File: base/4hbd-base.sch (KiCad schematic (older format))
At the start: 13 parts

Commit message: draft 0.02 of mosfets_sens_isol.sch
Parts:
- gave numbers to parts that had none: 13
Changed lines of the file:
@@
 $EndSheet
 $Comp
-L GNDD #PWR?
+L GNDD #PWR8
 U 1 1 5A1C4DF7
 P 8900 6000
-F 0 "#PWR?" H 8900 5750 50  0001 C CNN
+F 0 "#PWR8" H 8900 5750 50  0001 C CNN
 F 1 "GNDD" H 8900 5875 50  0000 C CNN
 F 2 "" H 8900 6000 50  0001 C CNN
@@
 $EndComp
 $Comp
-L GNDD #PWR?
+L GNDD #PWR7
 U 1 1 5A1C5052
 P 8900 3500
-F 0 "#PWR?" H 8900 3250 50  0001 C CNN
+F 0 "#PWR7" H 8900 3250 50  0001 C CNN
 F 1 "GNDD" H 8900 3375 50  0000 C CNN
 F 2 "" H 8900 3500 50  0001 C CNN
@@
 $EndComp
 $Comp
-L GNDD #PWR?
+L GNDD #PWR5
 U 1 1 5A1C5445
 P 4800 6300
-F 0 "#PWR?" H 4800 6050 50  0001 C CNN
+F 0 "#PWR5" H 4800 6050 50  0001 C CNN
 F 1 "GNDD" H 4800 6175 50  0000 C CNN
 F 2 "" H 4800 6300 50  0001 C CNN
@@
 $EndComp
 $Comp
-L GNDD #PWR?
+L GNDD #PWR4
 U 1 1 5A1C7749
 P 4800 3800
-F 0 "#PWR?" H 4800 3550 50  0001 C CNN
+F 0 "#PWR4" H 4800 3550 50  0001 C CNN
 F 1 "GNDD" H 4800 3675 50  0000 C CNN
 F 2 "" H 4800 3800 50  0001 C CNN
@@
 $EndComp
 $Comp
-L GNDD #PWR?
+L GNDD #PWR6
 U 1 1 5A1D2700
 P 8400 4800
-F 0 "#PWR?" H 8400 4550 50  0001 C CNN
+F 0 "#PWR6" H 8400 4550 50  0001 C CNN
 F 1 "GNDD" H 8400 4675 50  0000 C CNN
 F 2 "" H 8400 4800 50  0001 C CNN
@@
 $EndComp
 $Comp
-L Screw_Terminal_01x02 J?
+L Screw_Terminal_01x02 J11
 U 1 1 5A1D730D
 P 10800 5400
-F 0 "J?" H 10800 5500 50  0000 C CNN
+F 0 "J11" H 10800 5500 50  0000 C CNN
 F 1 "Screw_Terminal_01x02" H 10800 5200 50  0000 C CNN
 F 2 "" H 10800 5400 50  0001 C CNN
@@
 $EndComp
 $Comp
-L GNDD #PWR?
+L GNDD #PWR10
 U 1 1 5A1D7E7F
 P 10500 5500
-F 0 "#PWR?" H 10500 5250 50  0001 C CNN
+F 0 "#PWR10" H 10500 5250 50  0001 C CNN
 F 1 "GNDD" H 10500 5375 50  0000 C CNN
 F 2 "" H 10500 5500 50  0001 C CNN
@@
 $EndSheet
 $Comp
-L Conn_01x08 J?
+L Conn_01x08 J13
 U 1 1 5A1E2A64
 P 10900 2700
-F 0 "J?" H 10900 3100 50  0000 C CNN
+F 0 "J13" H 10900 3100 50  0000 C CNN
 F 1 "Conn_01x08" H 10900 2200 50  0000 C CNN
 F 2 "" H 10900 2700 50  0001 C CNN
@@
 $EndComp
 $Comp
-L GNDD #PWR?
+L GNDD #PWR11
 U 1 1 5A1E3D1F
 P 10600 2500
-F 0 "#PWR?" H 10600 2250 50  0001 C CNN
+F 0 "#PWR11" H 10600 2250 50  0001 C CNN
 F 1 "GNDD" H 10600 2375 50  0000 C CNN
 F 2 "" H 10600 2500 50  0001 C CNN
@@
 $EndComp
 $Comp
-L GNDD #PWR?
+L GNDD #PWR9
 U 1 1 5A1E950D
 P 10200 1600
-F 0 "#PWR?" H 10200 1350 50  0001 C CNN
+F 0 "#PWR9" H 10200 1350 50  0001 C CNN
 F 1 "GNDD" H 10200 1475 50  0000 C CNN
 F 2 "" H 10200 1600 50  0001 C CNN
@@
 Connection ~ 10400 5400
 $Comp
-L Conn_01x03 J?
+L Conn_01x03 J12
 U 1 1 5A1EF510
 P 10900 1100
-F 0 "J?" H 10900 1300 50  0000 C CNN
+F 0 "J12" H 10900 1300 50  0000 C CNN
 F 1 "Conn_01x03" H 10900 900 50  0000 C CNN
 F 2 "" H 10900 1100 50  0001 C CNN
@@
 	1400 7000 1200 7000
 $Comp
-L GNDPWR #PWR?
+L GNDPWR #PWR3
 U 1 1 5A1F43A1
 P 2800 6300
-F 0 "#PWR?" H 2800 6100 50  0001 C CNN
+F 0 "#PWR3" H 2800 6100 50  0001 C CNN
 F 1 "GNDPWR" H 2800 6170 50  0000 C CNN
 F 2 "" H 2800 6250 50  0001 C CNN
@@
 $EndComp
 $Comp
-L GNDPWR #PWR?
+L GNDPWR #PWR1
 U 1 1 5A1F4674
 P 1200 7100
-F 0 "#PWR?" H 1200 6900 50  0001 C CNN
+F 0 "#PWR1" H 1200 6900 50  0001 C CNN
 F 1 "GNDPWR" H 1200 6970 50  0000 C CNN
 F 2 "" H 1200 7050 50  0001 C CNN
@@
 $EndComp
 $Comp
-L GNDPWR #PWR?
+L GNDPWR #PWR2
 U 1 1 5A1F4ECF
 P 2800 3600
-F 0 "#PWR?" H 2800 3400 50  0001 C CNN
+F 0 "#PWR2" H 2800 3400 50  0001 C CNN
 F 1 "GNDPWR" H 2800 3470 50  0000 C CNN
 F 2 "" H 2800 3550 50  0001 C CNN
@@
 	2500 3300 3000 3300
 $Comp
-L Screw_Terminal_01x03 J?
+L Screw_Terminal_01x03 J9
 U 1 1 5A1F5775
 P 700 6700
-F 0 "J?" H 700 6900 50  0000 C CNN
+F 0 "J9" H 700 6900 50  0000 C CNN
 F 1 "Screw_Terminal_01x03" H 700 6500 50  0000 C CNN
 F 2 "" H 700 6700 50  0001 C CNN
@@
 	1100 3200 3000 3200
 $Comp
-L Screw_Terminal_01x04 J?
+L Screw_Terminal_01x04 J10
 U 1 1 5A1F75AA
 P 2400 1900
-F 0 "J?" H 2400 2100 50  0000 C CNN
+F 0 "J10" H 2400 2100 50  0000 C CNN
 F 1 "Screw_Terminal_01x04" H 2400 1600 50  0000 C CNN
 F 2 "" H 2400 1900 50  0001 C CNN
@@
 	2600 2000 3000 2000
 $Comp
-L Screw_Terminal_01x03 J?
+L Screw_Terminal_01x03 J1
 U 1 1 5A1F8DA5
 P 700 3400
-F 0 "J?" H 700 3600 50  0000 C CNN
+F 0 "J1" H 700 3600 50  0000 C CNN
 F 1 "Screw_Terminal_01x03" H 700 3200 50  0000 C CNN
 F 2 "" H 700 3400 50  0001 C CNN
@@
 $EndComp
 $Comp
-L Screw_Terminal_01x03 J?
+L Screw_Terminal_01x03 J2
 U 1 1 5A1F90C1
 P 700 3800
-F 0 "J?" H 700 4000 50  0000 C CNN
+F 0 "J2" H 700 4000 50  0000 C CNN
 F 1 "Screw_Terminal_01x03" H 700 3600 50  0000 C CNN
 F 2 "" H 700 3800 50  0001 C CNN
@@
 $EndComp
 $Comp
-L Screw_Terminal_01x03 J?
+L Screw_Terminal_01x03 J3
 U 1 1 5A1F93B8
 P 700 4200
-F 0 "J?" H 700 4400 50  0000 C CNN
+F 0 "J3" H 700 4400 50  0000 C CNN
 F 1 "Screw_Terminal_01x03" H 700 4000 50  0000 C CNN
 F 2 "" H 700 4200 50  0001 C CNN
@@
 $EndComp
 $Comp
-L Screw_Terminal_01x03 J?
+L Screw_Terminal_01x03 J4
 U 1 1 5A1F96AE
 P 700 4600
-F 0 "J?" H 700 4800 50  0000 C CNN
+F 0 "J4" H 700 4800 50  0000 C CNN
 F 1 "Screw_Terminal_01x03" H 700 4400 50  0000 C CNN
 F 2 "" H 700 4600 50  0001 C CNN
@@
 $EndComp
 $Comp
-L Screw_Terminal_01x03 J?
+L Screw_Terminal_01x03 J8
 U 1 1 5A1F99A1
 P 700 6000
-F 0 "J?" H 700 6200 50  0000 C CNN
+F 0 "J8" H 700 6200 50  0000 C CNN
 F 1 "Screw_Terminal_01x03" H 700 5800 50  0000 C CNN
 F 2 "" H 700 6000 50  0001 C CNN
@@
 $EndComp
 $Comp
-L Screw_Terminal_01x03 J?
+L Screw_Terminal_01x03 J7
 U 1 1 5A1F9CC3
 P 700 5600
-F 0 "J?" H 700 5800 50  0000 C CNN
+F 0 "J7" H 700 5800 50  0000 C CNN
 F 1 "Screw_Terminal_01x03" H 700 5400 50  0000 C CNN
 F 2 "" H 700 5600 50  0001 C CNN
@@
 $EndComp
 $Comp
-L Screw_Terminal_01x02 J?
+L Screw_Terminal_01x02 J5
 U 1 1 5A1FA292
 P 700 5000
-F 0 "J?" H 700 5100 50  0000 C CNN
+F 0 "J5" H 700 5100 50  0000 C CNN
 F 1 "Screw_Terminal_01x02" H 700 4800 50  0000 C CNN
 F 2 "" H 700 5000 50  0001 C CNN
@@
 $EndComp
 $Comp
-L Screw_Terminal_01x02 J?
+L Screw_Terminal_01x02 J6
 U 1 1 5A1FAA40
 P 700 5300
-F 0 "J?" H 700 5400 50  0000 C CNN
+F 0 "J6" H 700 5400 50  0000 C CNN
 F 1 "Screw_Terminal_01x02" H 700 5100 50  0000 C CNN
 F 2 "" H 700 5300 50  0001 C CNN

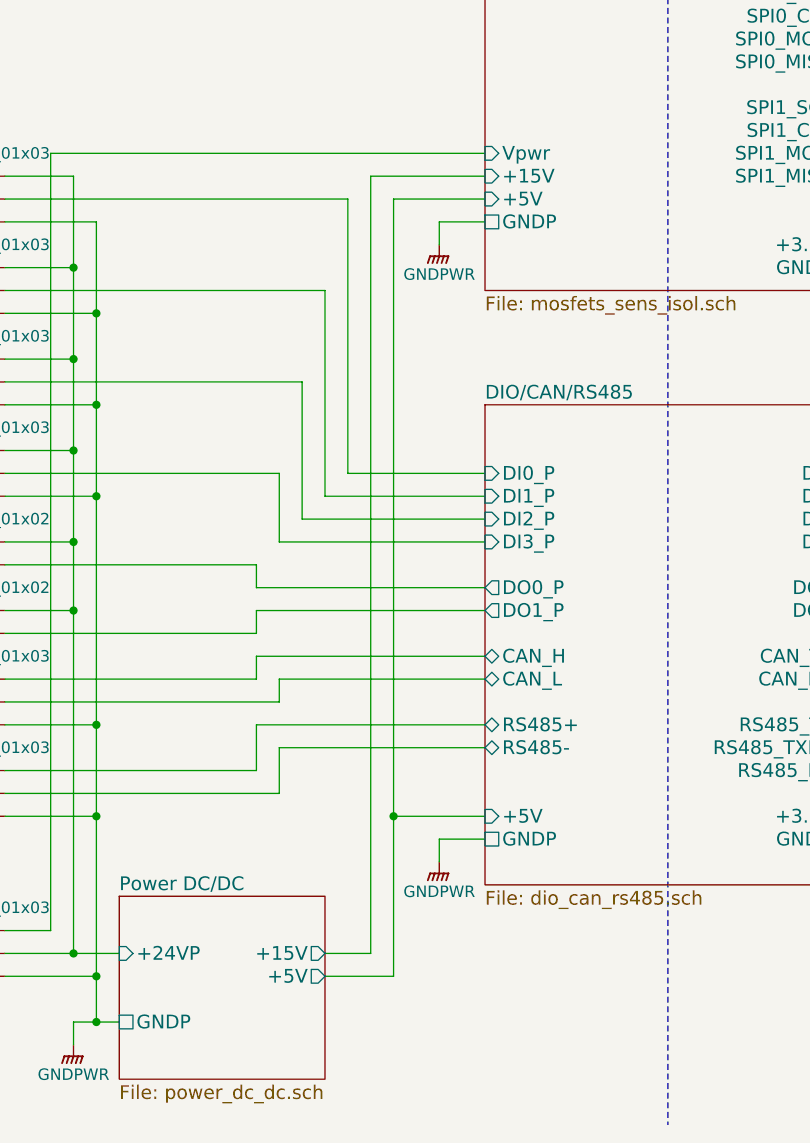
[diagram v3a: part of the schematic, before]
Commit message: draft 0.03 of mosfets_sens_isol.sch
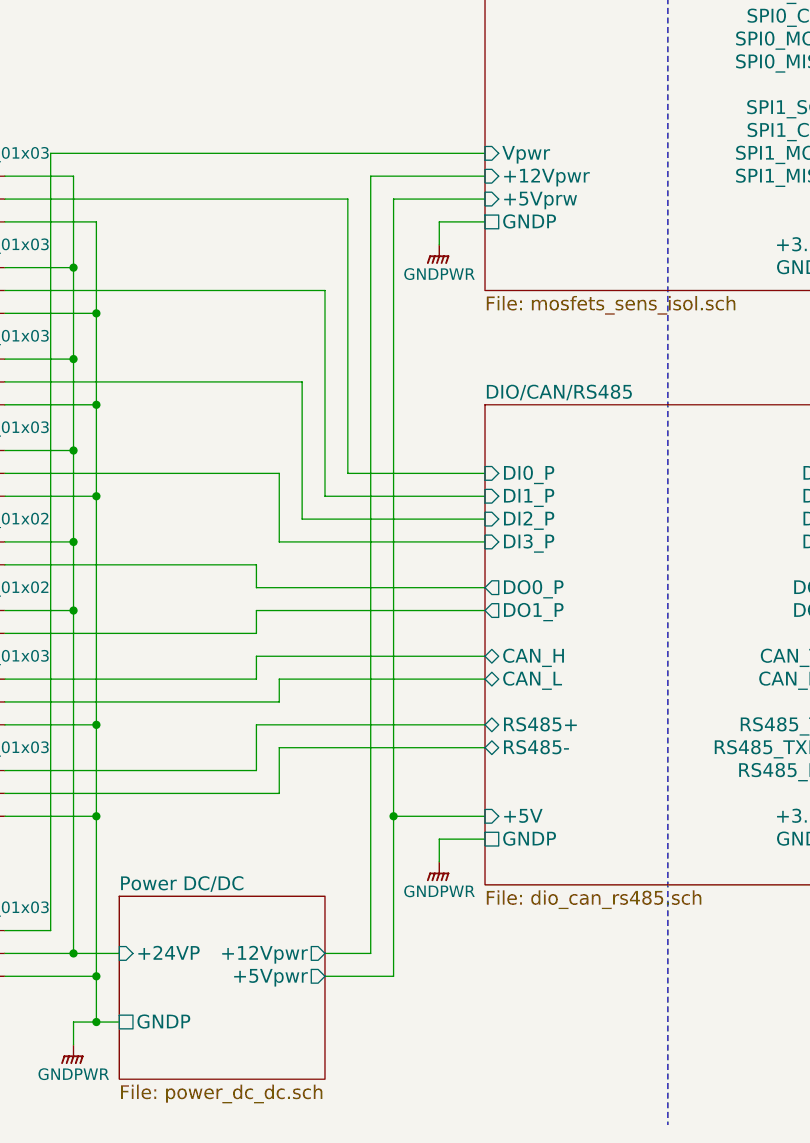
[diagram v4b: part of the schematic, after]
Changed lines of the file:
@@
 LIBS:ir
 LIBS:power
+LIBS:analog_devices
+LIBS:nxp
+LIBS:Logic_74xx
 LIBS:4hbd-base-cache
 EELAYER 25 0
@@
 F23 "GNDD" U R 4600 3700 60
 F24 "Vpwr" I L 3000 3200 60
-F25 "+15V" I L 3000 3300 60
-F26 "+5V" I L 3000 3400 60
+F25 "+12Vpwr" I L 3000 3300 60
+F26 "+5Vprw" I L 3000 3400 60
 F27 "GNDP" U L 3000 3500 60
 $EndSheet
@@
 F1 "power_dc_dc.sch" 60
 F2 "+24VP" I L 1400 6700 60
-F3 "+15V" O R 2300 6700 60
-F4 "+5V" O R 2300 6800 60
+F3 "+12Vpwr" O R 2300 6700 60
+F4 "+5Vpwr" O R 2300 6800 60
 F5 "GNDP" U L 1400 7000 60
 $EndSheet

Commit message: draf 0.1 of mosfets_sens_isol.sch
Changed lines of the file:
@@
 LIBS:nxp
 LIBS:Logic_74xx
+LIBS:silabs
 LIBS:4hbd-base-cache
 EELAYER 25 0
@@
 	4800 3700 4800 3800
 Wire Wire Line
-	9100 5300 8600 5300
+	5100 5300 8600 5300
+Wire Wire Line
+	8600 5300 9100 5300
 Wire Wire Line
 	8600 5300 8600 4600
@@
 	6500 5500 6500 6100
 Wire Wire Line
-	6500 6100 4600 6100
+	6500 6100 5000 6100
+Wire Wire Line
+	5000 6100 4600 6100
 Wire Wire Line
 	4600 3600 5000 3600
@@
 	9100 2900 8200 2900
 Wire Wire Line
-	10300 5400 10600 5400
+	10300 5400 10400 5400
+Wire Wire Line
+	10400 5400 10600 5400
 Wire Wire Line
 	10600 5500 10500 5500
@@
 	5900 4100 6900 4100
 Wire Wire Line
-	6500 5500 9100 5500
+	6500 5500 8700 5500
+Wire Wire Line
+	8700 5500 9100 5500
 Wire Wire Line
 	6000 4300 6900 4300
@@
 	2800 6200 2800 6300
 Wire Wire Line
-	1400 7000 1200 7000
+	1400 7000 1300 7000
+Wire Wire Line
+	1300 7000 1200 7000
 $Comp
 L GNDPWR #PWR3
@@
 	2600 6800 2300 6800
 Wire Wire Line
-	2600 3400 2600 6800
+	2600 3400 2600 6100
+Wire Wire Line
+	2600 6100 2600 6800
 Wire Wire Line
 	2600 6100 3000 6100
@@
 	900  6800 1300 6800
 Wire Wire Line
-	900  6700 1400 6700
+	900  6700 1200 6700
+Wire Wire Line
+	1200 6700 1400 6700
 Wire Wire Line
 	900  6600 1100 6600
@@
 	1200 7000 1200 7100
 Wire Wire Line
-	1300 3500 1300 7000
+	1300 3500 1300 3900
+Wire Wire Line
+	1300 3900 1300 4300
+Wire Wire Line
+	1300 4300 1300 4700
+Wire Wire Line
+	1300 4700 1300 5700
+Wire Wire Line
+	1300 5700 1300 6100
+Wire Wire Line
+	1300 6100 1300 6800
+Wire Wire Line
+	1300 6800 1300 7000
 Connection ~ 1300 7000
 Wire Wire Line
@@
 Connection ~ 1300 6100
 Wire Wire Line
-	1200 3300 1200 6700
+	1200 3300 1200 3700
+Wire Wire Line
+	1200 3700 1200 4100
+Wire Wire Line
+	1200 4100 1200 4500
+Wire Wire Line
+	1200 4500 1200 4900
+Wire Wire Line
+	1200 4900 1200 5200
+Wire Wire Line
+	1200 5200 1200 6700
 Wire Wire Line
 	1200 5200 900  5200
@@
 Wire Wire Line
 	2100 6000 900  6000
+Wire Wire Line
+	5100 5300 5100 3500
+Wire Wire Line
+	5100 3500 4600 3500
+Connection ~ 8600 5300
+Text HLabel 4600 3500 0    60   Input ~ 0
++5V
 $EndSCHEMATC

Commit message: Implement digital DC/DC convertor page.
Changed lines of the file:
@@
 LIBS:power
 LIBS:analog_devices
-LIBS:nxp
-LIBS:Logic_74xx
 LIBS:silabs
+LIBS:dc-dc
+LIBS:regul
 LIBS:4hbd-base-cache
 EELAYER 25 0
@@
 	4800 3700 4800 3800
 Wire Wire Line
-	5100 5300 8600 5300
-Wire Wire Line
-	8600 5300 9100 5300
+	5100 5300 9100 5300
 Wire Wire Line
 	8600 5300 8600 4600
@@
 	6400 5900 6400 4800
 Wire Wire Line
-	6500 5500 6500 6100
-Wire Wire Line
-	6500 6100 5000 6100
-Wire Wire Line
-	5000 6100 4600 6100
+	6500 6100 6500 5500
+Wire Wire Line
+	4600 6100 6500 6100
 Wire Wire Line
 	4600 3600 5000 3600
@@
 	9100 2900 8200 2900
 Wire Wire Line
-	10300 5400 10400 5400
-Wire Wire Line
-	10400 5400 10600 5400
+	10300 5400 10600 5400
 Wire Wire Line
 	10600 5500 10500 5500
@@
 	5900 4100 6900 4100
 Wire Wire Line
-	6500 5500 8700 5500
-Wire Wire Line
-	8700 5500 9100 5500
+	6500 5500 9100 5500
 Wire Wire Line
 	6000 4300 6900 4300
@@
 	2800 6200 2800 6300
 Wire Wire Line
-	1400 7000 1300 7000
-Wire Wire Line
-	1300 7000 1200 7000
+	1200 7000 1400 7000
 $Comp
 L GNDPWR #PWR3
@@
 	2600 6800 2300 6800
 Wire Wire Line
-	2600 3400 2600 6100
-Wire Wire Line
-	2600 6100 2600 6800
+	2600 3400 2600 6800
 Wire Wire Line
 	2600 6100 3000 6100
@@
 $EndComp
 Wire Wire Line
-	900  6800 1300 6800
-Wire Wire Line
-	900  6700 1200 6700
-Wire Wire Line
-	1200 6700 1400 6700
+	1300 6800 900  6800
+Wire Wire Line
+	900  6700 1400 6700
 Wire Wire Line
 	900  6600 1100 6600
@@
 	1200 7000 1200 7100
 Wire Wire Line
-	1300 3500 1300 3900
-Wire Wire Line
-	1300 3900 1300 4300
-Wire Wire Line
-	1300 4300 1300 4700
-Wire Wire Line
-	1300 4700 1300 5700
-Wire Wire Line
-	1300 5700 1300 6100
-Wire Wire Line
-	1300 6100 1300 6800
-Wire Wire Line
-	1300 6800 1300 7000
+	1300 3500 1300 7000
 Connection ~ 1300 7000
 Wire Wire Line
@@
 Connection ~ 1300 6100
 Wire Wire Line
-	1200 3300 1200 3700
-Wire Wire Line
-	1200 3700 1200 4100
-Wire Wire Line
-	1200 4100 1200 4500
-Wire Wire Line
-	1200 4500 1200 4900
-Wire Wire Line
-	1200 4900 1200 5200
-Wire Wire Line
-	1200 5200 1200 6700
+	1200 3300 1200 6700
 Wire Wire Line
 	1200 5200 900  5200
